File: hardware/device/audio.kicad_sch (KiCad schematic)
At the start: 6 parts, among them J10 MIDI_OUT, J6 LINE_IN, J8 LINE_OUT, J9 MIDI_IN

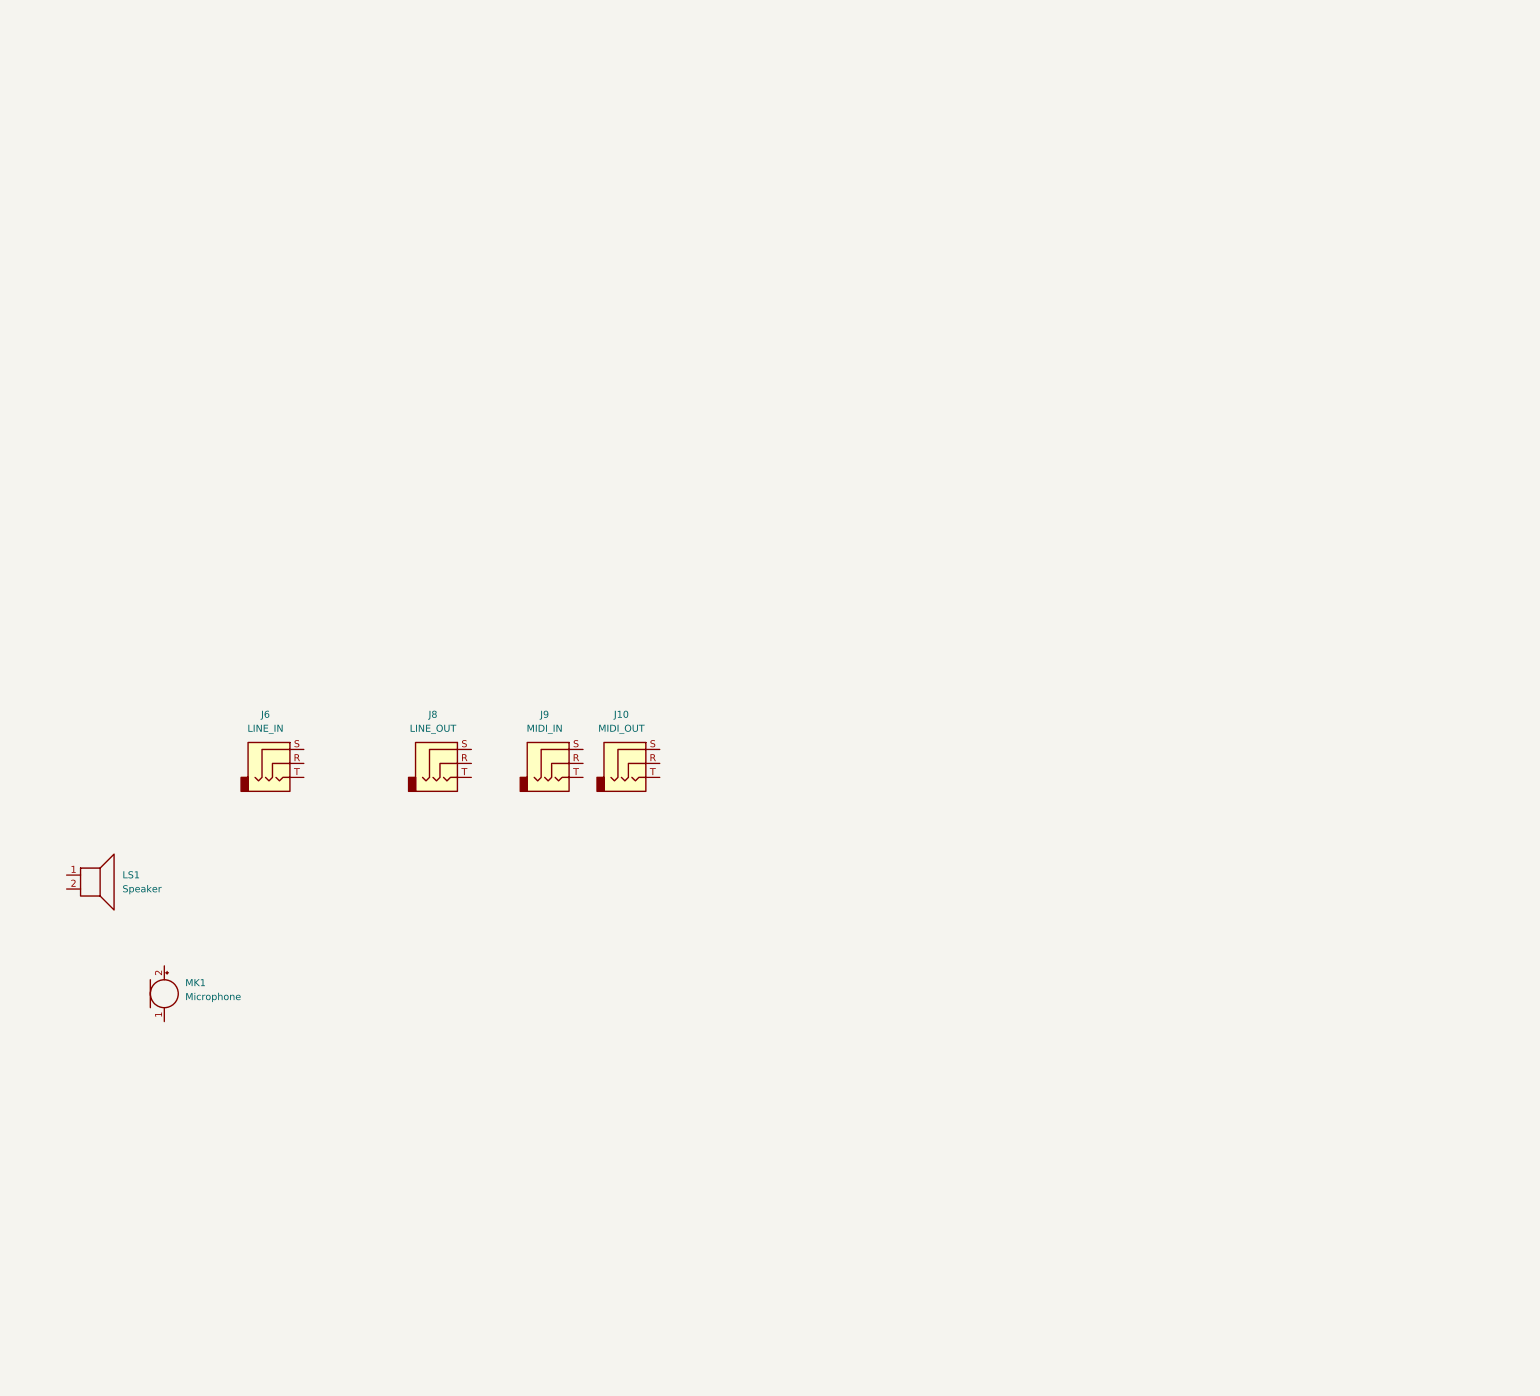
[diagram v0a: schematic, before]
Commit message: feat: audio schematic, FMC bus, SDRAM connections
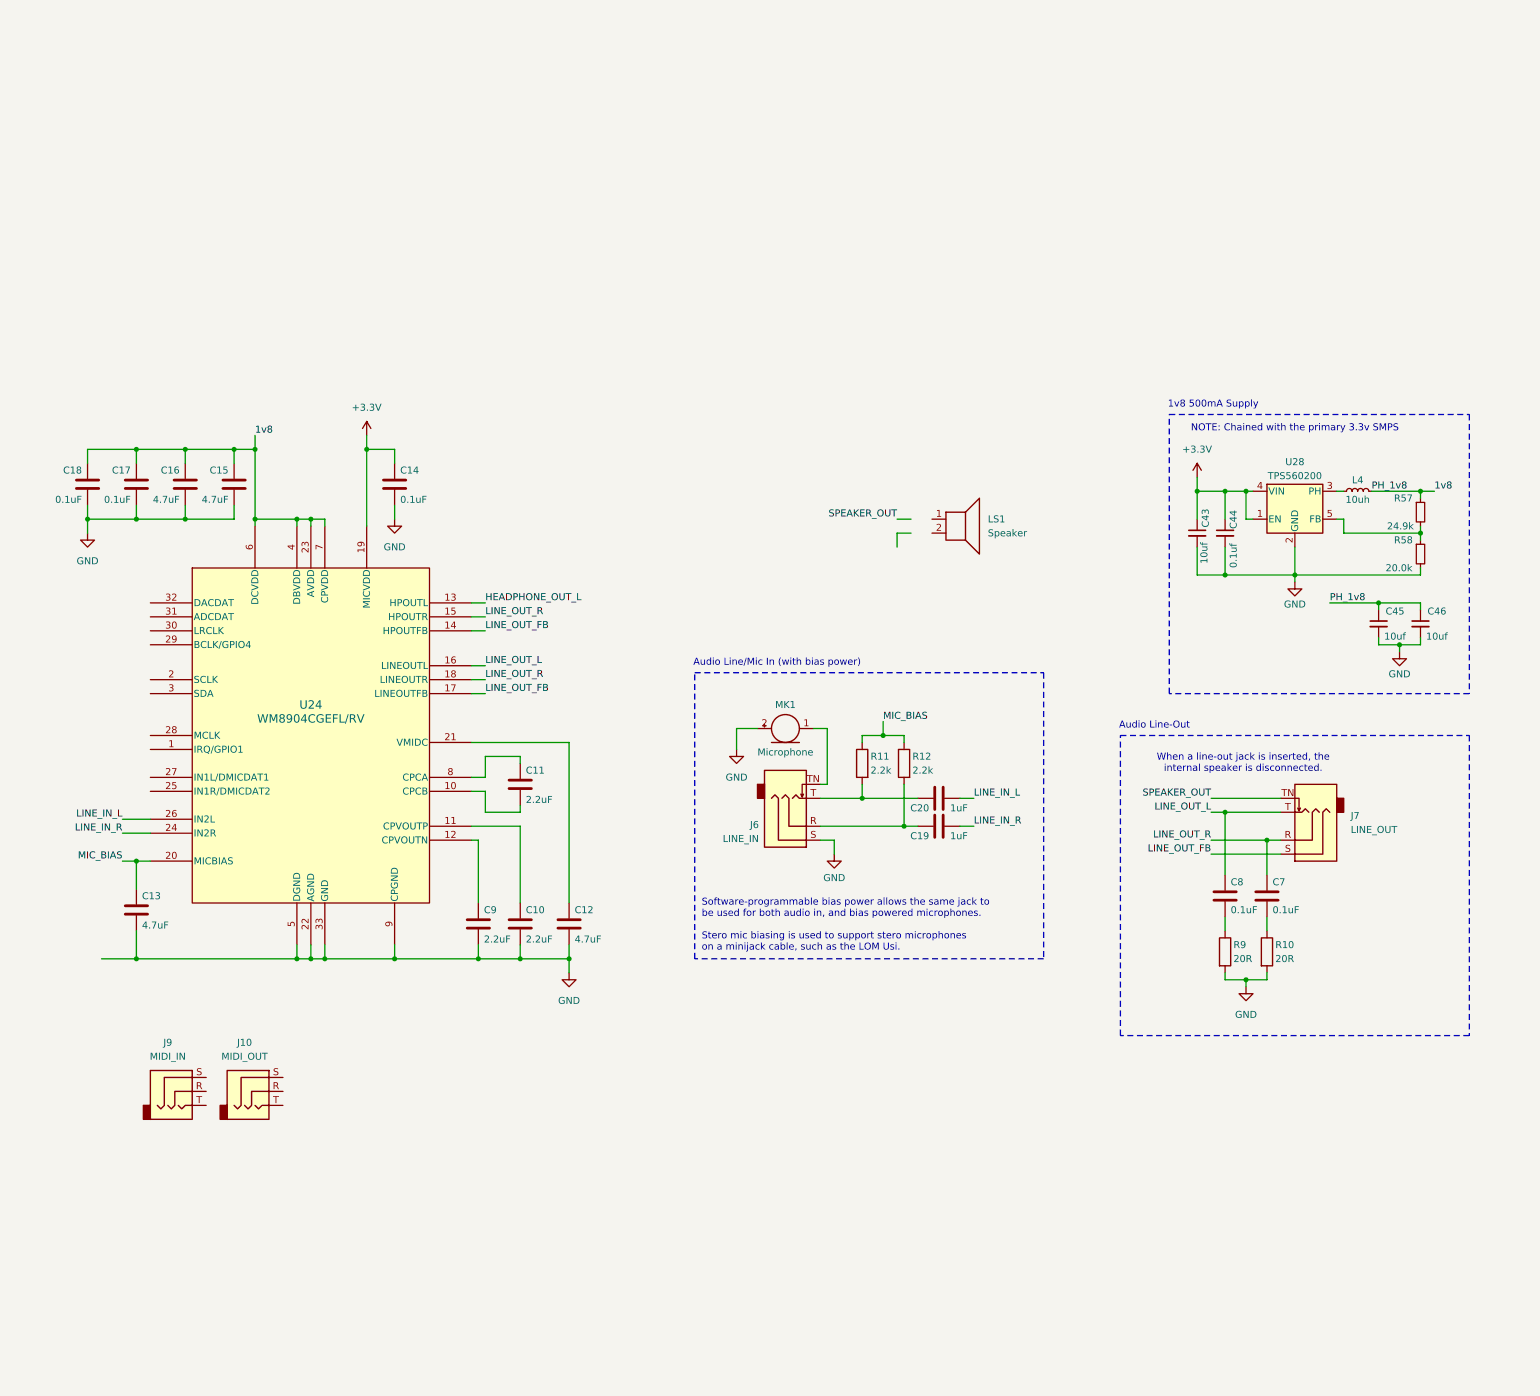
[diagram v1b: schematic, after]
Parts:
- removed J6: LINE_IN, Connector_Audio:Jack_3.5mm_CUI_SJ-3523-SMT_Horizontal, symbol Connector_Audio:AudioJack3
- removed J8: LINE_OUT, Connector_Audio:Jack_3.5mm_CUI_SJ-3523-SMT_Horizontal, symbol Connector_Audio:AudioJack3
- added C10, C11, C9: 2.2uF, Capacitor_SMD:C_0603_1608Metric_Pad1.08x0.95mm_HandSolder, symbol Device:C
- added C12, C13, C15, C16: 4.7uF, Capacitor_SMD:C_0603_1608Metric_Pad1.08x0.95mm_HandSolder, symbol Device:C
- added C14, C17, C18, C7, C8: 0.1uF, Capacitor_SMD:C_0603_1608Metric_Pad1.08x0.95mm_HandSolder, symbol Device:C
- added C19, C20: 1uF, Capacitor_SMD:C_0603_1608Metric_Pad1.08x0.95mm_HandSolder, symbol Device:C
- added C43, C45, C46: 10uf, Capacitor_SMD:C_0603_1608Metric_Pad1.08x0.95mm_HandSolder, symbol Device:C_Small
- added C44: 0.1uf, Capacitor_SMD:C_0603_1608Metric_Pad1.08x0.95mm_HandSolder, symbol Device:C_Small
- added J6: LINE_IN, Connector_Audio:Jack_3.5mm_CUI_SJ-3524-SMT_Horizontal, symbol Connector_Audio:AudioJack3_SwitchT
- added J7: LINE_OUT, Connector_Audio:Jack_3.5mm_CUI_SJ-3524-SMT_Horizontal, symbol Connector_Audio:AudioJack3_SwitchT
- added L4: 10uh, symbol Device:L_Small
- added R10, R9: 20R, Resistor_SMD:R_0603_1608Metric_Pad0.98x0.95mm_HandSolder, symbol Device:R
- added R11, R12: 2.2k, symbol Device:R
- added R57: 24.9k, Resistor_SMD:R_0603_1608Metric_Pad0.98x0.95mm_HandSolder, symbol Device:R_Small
- added R58: 20.0k, Resistor_SMD:R_0603_1608Metric_Pad0.98x0.95mm_HandSolder, symbol Device:R_Small
- added U24: WM8904CGEFL/RV, pocket_synth:WM8904CGEFL_RV, symbol pocket_synth:WM8904CGEFL_RV
- added U28: TPS560200, Package_TO_SOT_SMD:SOT-23-5, symbol Regulator_Switching:TPS560200
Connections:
- net at MK1.1 (-): now also J6.TN
- net GND: now reaches MK1.2 (+)
- net GND: now also C10.2, C12.2, C13.2, C14.2, C15.2, C16.2, C17.2, C18.2, C43.2, C44.2, C45.2, C46.2, C9.2, J6.S, R10.2, R58.2, R9.2, U24.22 (AGND), U24.33 (GND), U24.5 (DGND), U24.9 (CPGND), U28.2 (GND)
- new net: C10.1, U24.11 (CPVOUTP)
- new net: R57.2, R58.1, U28.5 (FB)
- new net: C19.1, J6.R, R12.2
- new net: C20.1, J6.T, R11.2
- new net: C11.2, U24.10 (CPCB)
- new net: C9.1, U24.12 (CPVOUTN)
- new net: C12.1, U24.21 (VMIDC)
- new net: C11.1, U24.8 (CPCA)
- new net: L4.1, U28.3 (PH)
- new net: C8.2, R9.1
- new net: C7.2, R10.1
- new net +3.3V: C14.1, C43.1, C44.1, U24.19 (MICVDD), U28.1 (EN), U28.4 (VIN)
- new net 1v8: C15.1, C16.1, C17.1, C18.1, C45.1, C46.1, L4.2, R57.1, U24.23 (AVDD), U24.4 (DBVDD), U24.6 (DCVDD), U24.7 (CPVDD)
- new net HEADPHONE_OUT_L: U24.13 (HPOUTL)
- new net LINE_IN_L: C20.2, U24.26 (IN2L)
- new net LINE_IN_R: C19.2, U24.24 (IN2R)
- new net LINE_OUT_FB: J7.S, U24.14 (HPOUTFB), U24.17 (LINEOUTFB)
- new net LINE_OUT_L: C8.1, J7.T, U24.16 (LINEOUTL)
- new net LINE_OUT_R: C7.1, J7.R, U24.15 (HPOUTR), U24.18 (LINEOUTR)
- new net MIC_BIAS: C13.1, R11.1, R12.1, U24.20 (MICBIAS)
- new net SPEAKER_OUT: J7.TN
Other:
- note added: "1v8 500mA Supply"
- note added: "Audio Line-Out"
- note added: "Audio Line/Mic In (with bias power)"
- note added: "NOTE: Chained with the primary 3.3v SMPS"
- note added: "Software-programmable bias power allows the same jack to be used for both audio in, and bias powered microphones. Stero mic biasing is used to support stero microphones on a minijack cable, such as the LOM Usi."
- note added: "When a line-out jack is inserted, the internal speaker is disconnected."
- moved on the sheet: J10, J9, LS1, MK1

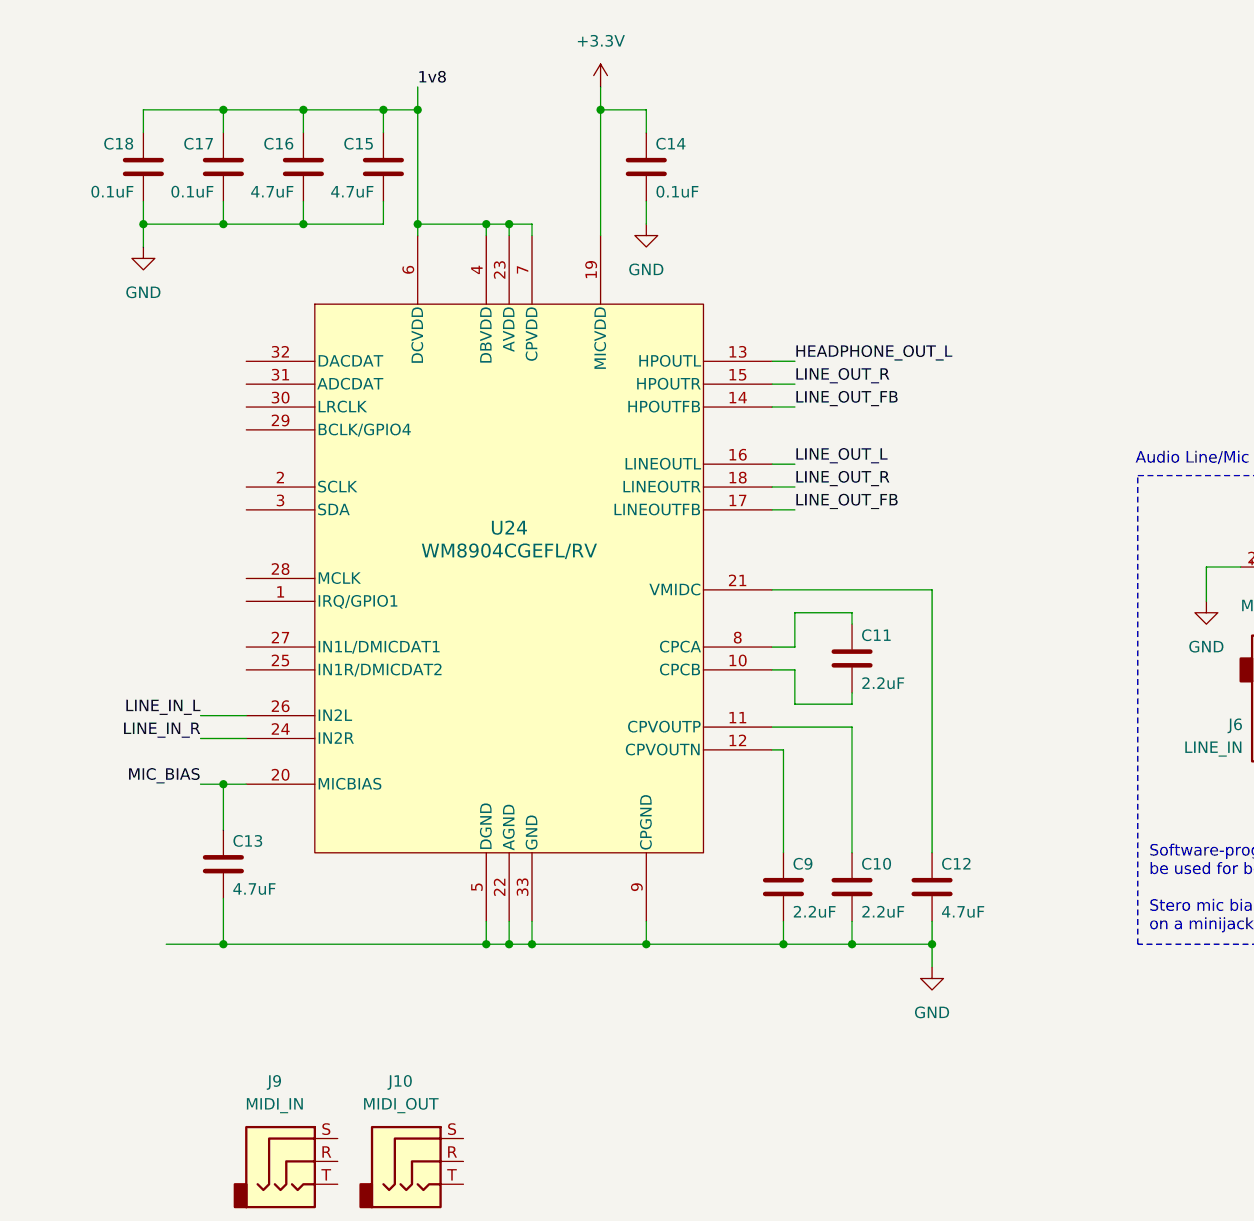
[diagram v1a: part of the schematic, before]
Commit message: feat: start codec layout
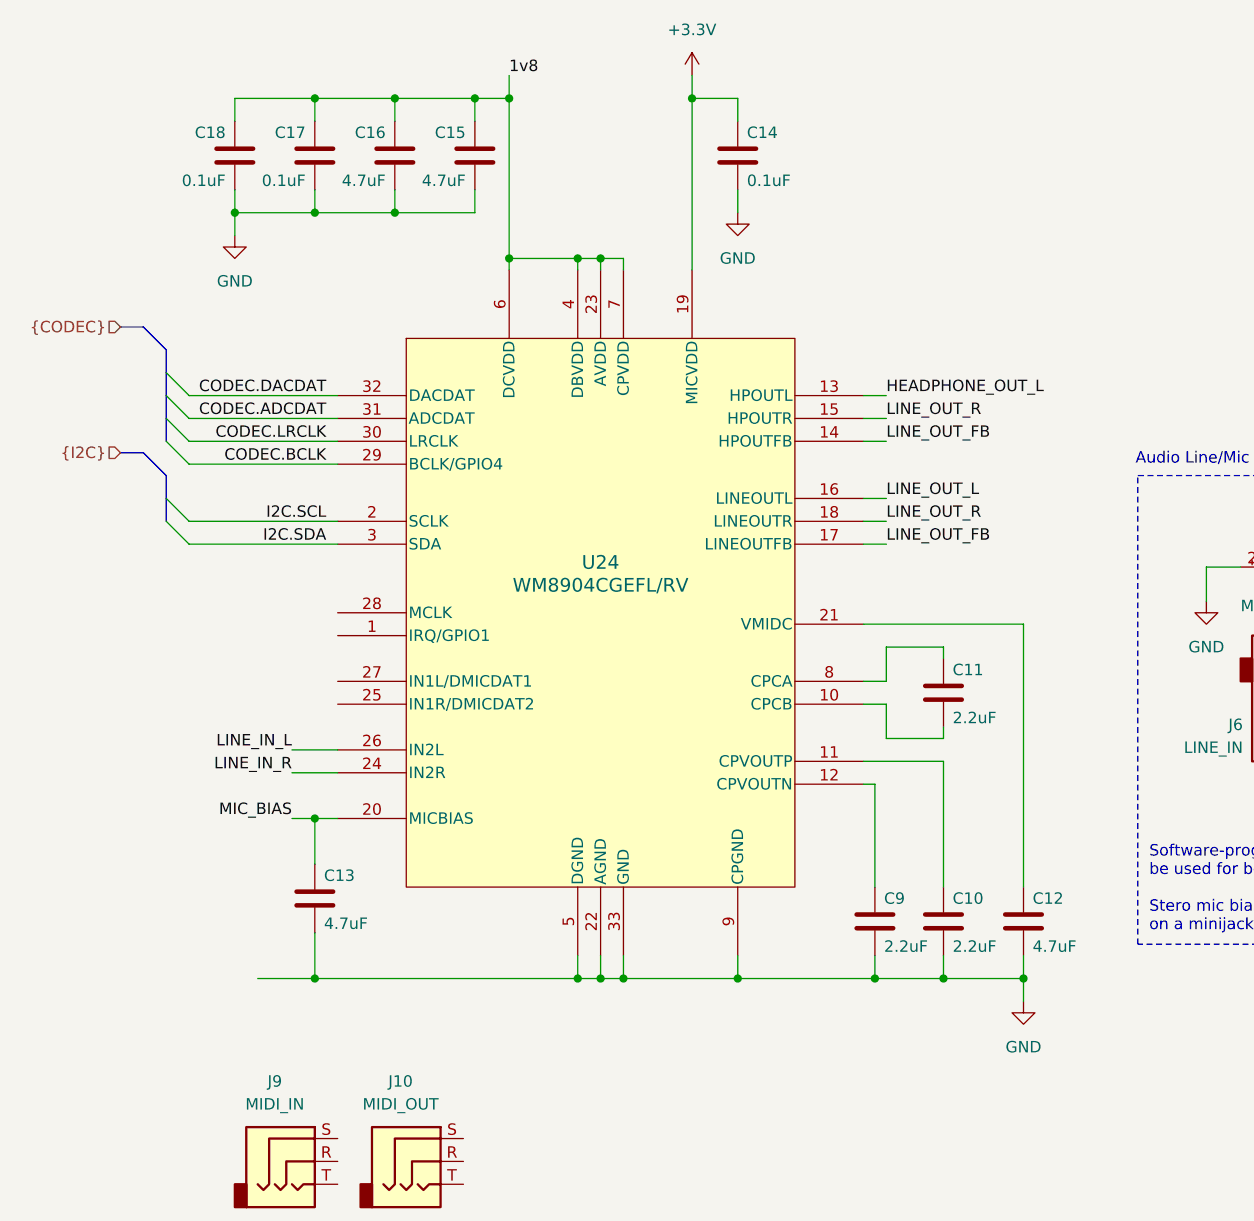
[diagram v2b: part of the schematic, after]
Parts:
- C10, C11, C12, C13, C14, C15, C16, C17, C18, C19, C20, C43, C44, C45, C46, C7, C8, C9: footprint Capacitor_SMD:C_0603_1608Metric_Pad1.08x0.95mm_HandSolder -> Capacitor_SMD:C_0402_1005Metric_Pad0.74x0.62mm_HandSolder
- R10, R9: footprint Resistor_SMD:R_0603_1608Metric_Pad0.98x0.95mm_HandSolder -> Resistor_SMD:R_0402_1005Metric_Pad0.72x0.64mm_HandSolder
- R11, R12: footprint (none) -> Capacitor_SMD:C_0402_1005Metric_Pad0.74x0.62mm_HandSolder
- R57, R58: footprint Resistor_SMD:R_0603_1608Metric_Pad0.98x0.95mm_HandSolder -> Capacitor_SMD:C_0402_1005Metric_Pad0.74x0.62mm_HandSolder
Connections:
- net I2C.SCL: now reaches U24.2 (SCLK)
- net CODEC.BCLK: now reaches U24.29 (BCLK/GPIO4)
- net I2C.SDA: now reaches U24.3 (SDA)
- net CODEC.LRCLK: now reaches U24.30 (LRCLK)
- net CODEC.ADCDAT: now reaches U24.31 (ADCDAT)
- net CODEC.DACDAT: now reaches U24.32 (DACDAT)
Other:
- moved on the sheet: C10, C11, C12, C13, C14, C15, C16, C17, C18, C9, U24

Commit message: feat: various layouts, changed SDRAM to BGA
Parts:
- removed C45: 10uf, Capacitor_SMD:C_0402_1005Metric_Pad0.74x0.62mm_HandSolder, symbol Device:C_Small
- removed J10: MIDI_OUT, Connector_Audio:Jack_3.5mm_CUI_SJ-3523-SMT_Horizontal, symbol Connector_Audio:AudioJack3
- removed J9: MIDI_IN, Connector_Audio:Jack_3.5mm_CUI_SJ-3523-SMT_Horizontal, symbol Connector_Audio:AudioJack3
- MK1: value Microphone -> MIC
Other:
- note added: "1v8 500mA Analog Audio Supply"
- note removed: "1v8 500mA Supply"
- moved on the sheet: C10, C11, C12, C13, C14, C15, C16, C17, C18, C19, C20, C43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

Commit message: feat: various audio and power schematic layout
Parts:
- added J5: AUDIO_MODULE, pocket_synth:FX6-20P-0.8SV1(71), symbol pocket_synth:FX6-20P-0.8SV1(71)
- added R18: 10k, symbol Device:R
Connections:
- net +3.3V: now also J5.1
- net CODEC.ADCDAT: now also J5.5
- net CODEC.BCLK: now also J5.9
- net CODEC.DACDAT: now also J5.3
- net CODEC.LRCLK: now also J5.7
- net GND: now also J5.19, R18.2
- net I2C.SCL: now also J5.13
- net I2C.SDA: now also J5.15
- net LINE_OUT_FB: now also J5.8; no longer U24.14 (HPOUTFB)
- net LINE_OUT_L: now also J5.4
- net LINE_OUT_R: now also J5.6; no longer U24.15 (HPOUTR)
- net CODEC_IRQ: now reaches U24.1 (IRQ/GPIO1)
- net CODEC.MCLK: now reaches U24.28 (MCLK)
- net CODEC.MCLK: now also J5.11
- new net EXP_DETECT: J5.2, R18.1
- new net HEADPHONE_OUT_FB: U24.14 (HPOUTFB)
- new net HEADPHONE_OUT_R: U24.15 (HPOUTR)
- no-connect marks 0 -> 2
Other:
- note added: "Expansion pulls HIGH to signal presence"
